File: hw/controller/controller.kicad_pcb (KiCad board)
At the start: 2 copper layers, 67.3 x 76.2 mm, 61 parts, among them J1 ARM-SWD, P1 USB_OTG, P10 GPIO, P11 VDD_SEL, P12 UART0, P13 SPI, P14 I2C0, P15 I2C1, P16 I2C2, P17 I2C3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

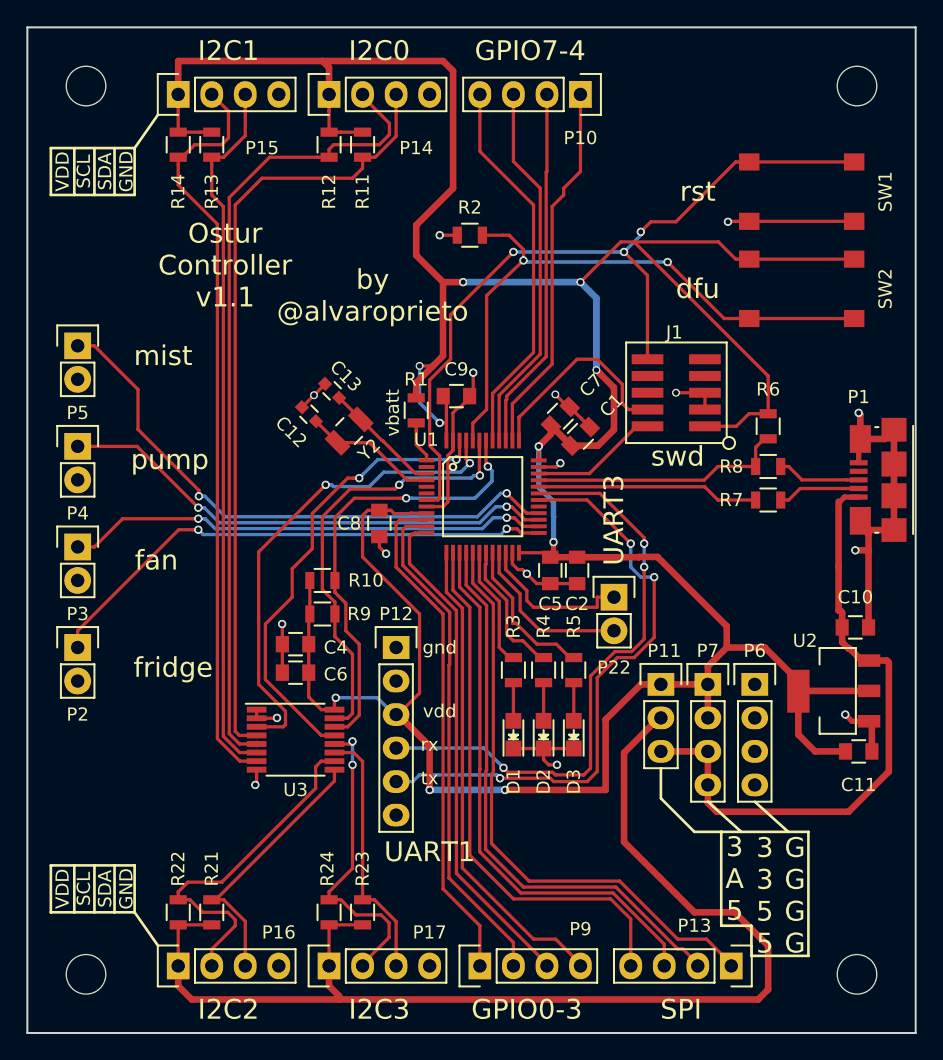
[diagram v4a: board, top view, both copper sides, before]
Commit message: Updating ostur controller!
Removed unused headers
Added extra shielding for 32768Hz crystal
Made board smaller
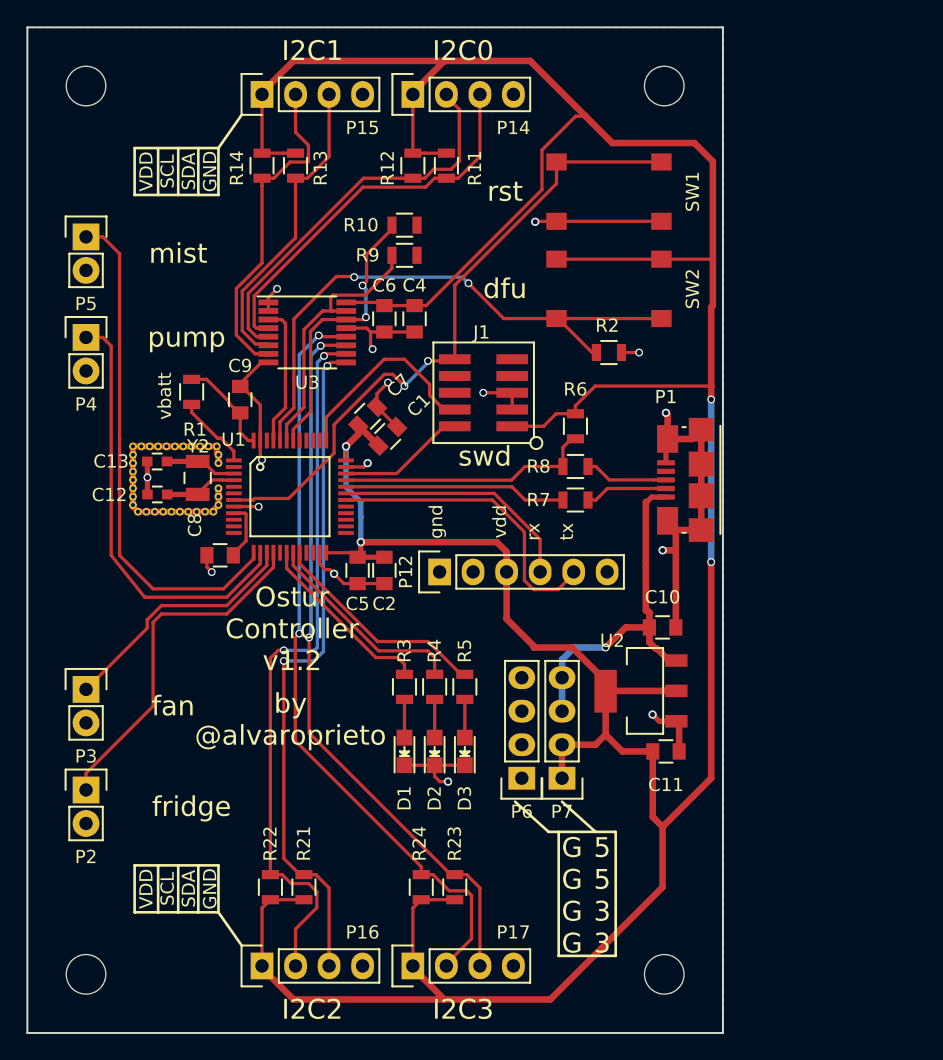
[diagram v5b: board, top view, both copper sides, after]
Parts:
- removed P10, P9: GPIO, Pin_Headers:Pin_Header_Straight_1x04
- removed P11: VDD_SEL, Pin_Headers:Pin_Header_Straight_1x03
- removed P13: SPI, Pin_Headers:Pin_Header_Straight_1x04
- removed P22: UART3, Pin_Headers:Pin_Header_Straight_1x02
- added REF**: via-0.6mm, footprints:via-0.6mm, F.Cu at (122.4, 109.2)
- added REF**: via-0.6mm, footprints:via-0.6mm, F.Cu at (117.9, 108.0)
- added REF**: via-0.6mm, footprints:via-0.6mm, F.Cu at (117.2, 108.0)
- added REF**: via-0.6mm, footprints:via-0.6mm, F.Cu at (116.6, 108.0)
- added REF**: via-0.6mm, footprints:via-0.6mm, F.Cu at (116.0, 108.0)
- added REF**: via-0.6mm, footprints:via-0.6mm, F.Cu at (116.0, 108.6)
- added REF**: via-0.6mm, footprints:via-0.6mm, F.Cu at (116.0, 109.2)
- added REF**: via-0.6mm, footprints:via-0.6mm, F.Cu at (116.0, 109.9)
- added REF**: via-0.6mm, footprints:via-0.6mm, F.Cu at (116.0, 110.5)
- added REF**: via-0.6mm, footprints:via-0.6mm, F.Cu at (116.0, 111.1)
- added REF**: via-0.6mm, footprints:via-0.6mm, F.Cu at (116.0, 111.8)
- added REF**: via-0.6mm, footprints:via-0.6mm, F.Cu at (122.4, 108.6)
- added REF**: via-0.6mm, footprints:via-0.6mm, F.Cu at (116.0, 112.4)
- added REF**: via-0.6mm, footprints:via-0.6mm, F.Cu at (116.3, 112.9)
- added REF**: via-0.6mm, footprints:via-0.6mm, F.Cu at (117.0, 112.9)
- added REF**: via-0.6mm, footprints:via-0.6mm, F.Cu at (117.6, 112.9)
- added REF**: via-0.6mm, footprints:via-0.6mm, F.Cu at (118.2, 112.9)
- added REF**: via-0.6mm, footprints:via-0.6mm, F.Cu at (118.9, 112.9)
- added REF**: via-0.6mm, footprints:via-0.6mm, F.Cu at (119.5, 112.9)
- added REF**: via-0.6mm, footprints:via-0.6mm, F.Cu at (120.1, 112.9)
- added REF**: via-0.6mm, footprints:via-0.6mm, F.Cu at (120.8, 112.9)
- added REF**: via-0.6mm, footprints:via-0.6mm, F.Cu at (122.0, 112.9)
- added REF**: via-0.6mm, footprints:via-0.6mm, F.Cu at (122.3, 108.0)
- added REF**: via-0.6mm, footprints:via-0.6mm, F.Cu at (122.4, 112.4)
- added REF**: via-0.6mm, footprints:via-0.6mm, F.Cu at (122.4, 111.8)
- added REF**: via-0.6mm, footprints:via-0.6mm, F.Cu at (122.4, 111.1)
- added REF**: via-0.6mm, footprints:via-0.6mm, F.Cu at (121.4, 112.9)
- added REF**: via-0.6mm, footprints:via-0.6mm, F.Cu at (121.7, 108.0)
- added REF**: via-0.6mm, footprints:via-0.6mm, F.Cu at (121.0, 108.0)
- added REF**: via-0.6mm, footprints:via-0.6mm, F.Cu at (120.4, 108.0)
- added REF**: via-0.6mm, footprints:via-0.6mm, F.Cu at (119.8, 108.0)
- added REF**: via-0.6mm, footprints:via-0.6mm, F.Cu at (119.1, 108.0)
- added REF**: via-0.6mm, footprints:via-0.6mm, F.Cu at (118.5, 108.0)
- C12, C13: value 12pF -> 6pF
- moved U3 30.9 mm to (129.2, 99.3)
- moved R9 27.9 mm to (136.5, 93.5), turned to 180 degrees
- moved C6 27.6 mm to (135.0, 98.3), turned to 270 degrees
- moved R10 27.6 mm to (136.5, 91.2), turned to 180 degrees
- moved C4 26.3 mm to (137.3, 98.3), turned to 270 degrees
- moved P6 19.0 mm to (145.4, 133.1), turned to 180 degrees
- moved R1 17.1 mm to (120.4, 103.8)
- moved C9 16.4 mm to (124.1, 104.4), turned to 90 degrees
- moved C1 14.6 mm to (135.3, 107.2)
- moved C11 14.6 mm to (156.3, 131.1)
- moved C5 14.6 mm to (133.0, 117.3)
- moved C7 14.6 mm to (133.7, 105.7)
- moved P1 14.6 mm to (156.3, 110.5)
- moved C10 14.6 mm to (156.1, 121.7)
- moved C2 14.6 mm to (135.0, 117.3)
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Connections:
- P16 pad 1: /VDD_ALT -> VDD
- P17 pad 1: /VDD_ALT -> VDD
- R21 pad 1: /VDD_ALT -> VDD
- R22 pad 1: /VDD_ALT -> VDD
- R23 pad 1: /VDD_ALT -> VDD
- R24 pad 1: /VDD_ALT -> VDD
- U1 pad 10: /GPIO0 -> Net-(U1-Pad10)
- U1 pad 11: /GPIO1 -> Net-(U1-Pad11)
- U1 pad 12: /GPIO2 -> Net-(U1-Pad12)
- U1 pad 13: /GPIO3 -> /MIST
- U1 pad 14: /CS -> /PUMP
- U1 pad 15: /SCK -> /FAN
- U1 pad 16: /MISO -> /FRIDGE
- U1 pad 17: /MOSI -> Net-(U1-Pad17)
- U1 pad 21: /UART3_TX -> Net-(U1-Pad21)
- U1 pad 22: /UART3_RX -> Net-(U1-Pad22)
- U1 pad 25: /FRIDGE -> Net-(U1-Pad25)
- U1 pad 26: /FAN -> Net-(U1-Pad26)
- U1 pad 27: /PUMP -> Net-(U1-Pad27)
- U1 pad 28: /MIST -> Net-(U1-Pad28)
- U1 pad 38: /GPIO4 -> Net-(U1-Pad38)
- U1 pad 39: /GPIO5 -> Net-(U1-Pad39)
- U1 pad 40: /GPIO6 -> Net-(U1-Pad40)
- U1 pad 41: /GPIO7 -> Net-(U1-Pad41)
- U1 pad 46: /TCA_A2 -> Net-(U1-Pad46)
- U3 pad 13: /TCA_A2 -> GND
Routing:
- net /VDD_ALT: track 89.3 -> 0.00 mm
- net /MOSI: track 44.8 -> 0.00 mm
- net /MISO: track 43.0 -> 0.00 mm
- net /SCK: track 41.8 -> 0.00 mm
- net /CS: track 41.2 -> 0.00 mm
- net /GPIO0: track 38.6 -> 0.00 mm
- net /GPIO1: track 38.5 -> 0.00 mm
- net /GPIO2: track 38.2 -> 0.00 mm
- net /GPIO3: track 36.5 -> 0.00 mm
- net /SDA3: track 19.5 -> 55.4 mm, vias 0 -> 2
- net /TCA_A2: track 35.2 -> 0.00 mm, vias 2 -> 0
- net /SCL3: track 23.6 -> 58.3 mm
- net /SCL1: track 57.5 -> 25.2 mm
- net /SDA2: track 20.5 -> 51.8 mm, vias 0 -> 2
- net /SCL0: track 61.4 -> 30.0 mm
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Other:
- board size 67.3 x 76.2 mm -> 52.7 x 76.2 mm
- board text added: "5 5 3 3"
- board text added: "Ostur Controller v1.2"
- board text removed: "3 3 5 5"
- board text removed: "3 A 5"
- board text removed: "GPIO0-3"
- board text removed: "GPIO7-4"
- board text removed: "Ostur Controller v1.1"
- board text removed: "SPI"
- board text removed: "UART1"
- board text removed: "UART3"

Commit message: Fixed controller PCB...
Somehow I forgot to connect some VDD lines on the micocontroller.....
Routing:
- net VDD: track 303.8 -> 325.5 mm, vias 4 -> 6
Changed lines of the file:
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@@
-(kicad_pcb (version 4) (host pcbnew 4.0.2+dfsg1-stable)
+(kicad_pcb (version 4) (host pcbnew 4.0.6-e0-6349~53~ubuntu16.04.1)
   (general
     (links 173)
-    (no_connects 4)
-    (area 107.874999 76.124999 160.730001 152.475001)
+    (no_connects 0)
+    (area 105.981474 75.6695 164.625046 154.03126)
     (thickness 1.6)
     (drawings 49)
-    (tracks 548)
+    (tracks 563)
     (zones 0)
     (modules 89)
@@
   (gr_line (start 160.655 152.4) (end 107.95 152.4) (layer Edge.Cuts) (width 0.15))
   (gr_line (start 160.655 76.2) (end 160.655 152.4) (layer Edge.Cuts) (width 0.15))
+  (segment (start 137.475 93.472) (end 137.475 91.186) (width 0.25) (layer F.Cu) (net 1))
+  (segment (start 137.287 97.282) (end 137.287 93.66) (width 0.25) (layer F.Cu) (net 1))
+  (segment (start 137.287 93.66) (end 137.475 93.472) (width 0.25) (layer F.Cu) (net 1))
+  (segment (start 124.719 113.284) (end 127 113.284) (width 0.25) (layer F.Cu) (net 1))
+  (segment (start 127 113.284) (end 129.54 113.284) (width 0.25) (layer F.Cu) (net 1))
+  (segment (start 127 112.776) (end 127 113.284) (width 0.25) (layer F.Cu) (net 1))
+  (segment (start 127 110.998) (end 127 112.776) (width 0.25) (layer B.Cu) (net 1))
+  (via (at 127 112.776) (size 0.6) (drill 0.4) (layers F.Cu B.Cu) (net 1))
+  (segment (start 125.095 110.109) (end 125.984 110.998) (width 0.25) (layer F.Cu) (net 1))
+  (segment (start 125.984 110.998) (end 127 110.998) (width 0.25) (layer F.Cu) (net 1))
+  (via (at 127 110.998) (size 0.6) (drill 0.4) (layers F.Cu B.Cu) (net 1))
+  (segment (start 125.095 107.51) (end 125.095 110.109) (width 0.25) (layer F.Cu) (net 1))
+  (segment (start 129.54 113.284) (end 130.595 114.339) (width 0.25) (layer F.Cu) (net 1))
+  (segment (start 130.595 114.339) (end 130.595 116.01) (width 0.25) (layer F.Cu) (net 1))
+  (segment (start 124.445 113.01) (end 124.719 113.284) (width 0.25) (layer F.Cu) (net 1))
   (segment (start 120.396 102.87) (end 121.539 102.87) (width 0.25) (layer F.Cu) (net 1))
   (segment (start 121.539 102.87) (end 123.204 104.535) (width 0.25) (layer F.Cu) (net 1))

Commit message: Fix merge screwup
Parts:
- removed P1: USB_OTG, footprints:USB_MICRO_B
- added J2: USB_OTG, footprints:USB_MICRO_B, F.Cu at (156.5, 110.5)

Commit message: Adding cheese wedges!
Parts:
- removed P12: UART0, Pin_Headers:Pin_Header_Straight_1x06
- added C14: 100nF, Capacitors_SMD:C_0603, F.Cu at (128.6, 86.6)
- added C15: 100nF, Capacitors_SMD:C_0603, F.Cu at (135.1, 118.3)
- added C16: 100nF, Capacitors_SMD:C_0603, F.Cu at (121.5, 97.6)
- added C17: 100nF, Capacitors_SMD:C_0603, F.Cu at (238.8, 72.4)
- added C3: 100nF, Capacitors_SMD:C_0603, F.Cu at (124.6, 111.0)
- added J3: UART, Pin_Headers:Pin_Header_Straight_1x03_Pitch1.27mm, F.Cu at (170.2, 90.2)
- added P1: TH0, Pin_Headers:Pin_Header_Straight_1x04_Pitch2.54mm, F.Cu at (105.7, 112.0)
- added P8: TH3, Pin_Headers:Pin_Header_Straight_1x04_Pitch2.54mm, F.Cu at (108.8, 83.4)
- added R15: 10k, Resistors_SMD:R_0603, F.Cu at (121.1, 109.6)
- added R16: DNP, Resistors_SMD:R_0603, F.Cu at (131.6, 82.5)
- added R17: 10k, Resistors_SMD:R_0603, F.Cu at (129.9, 83.3)
- added R18: DNP, Resistors_SMD:R_0603, F.Cu at (129.8, 118.6)
- added R19: 10k, Resistors_SMD:R_0603, F.Cu at (131.5, 119.4)
- added R20: DNP, Resistors_SMD:R_0603, F.Cu at (121.2, 92.3)
- added R25: 10k, Resistors_SMD:R_0603, F.Cu at (120.4, 94.0)
- added R26: DNP, Resistors_SMD:R_0603, F.Cu at (240.8, 83.8)
- added R27: DNP, Resistors_SMD:R_0603, F.Cu at (240.8, 80.0)
- added U4: SHT3x-DIS, footprints:SHT3x, F.Cu at (124.9, 107.1)
- added U5: SHT3x-DIS, footprints:SHT3x, F.Cu at (132.5, 87.0)
- added U6: SHT3x-DIS, footprints:SHT3x, F.Cu at (132.8, 115.1)
- added U7: SHT3x-DIS, footprints:SHT3x, F.Cu at (124.7, 95.4)
- added U8: SHT3x-DIS, footprints:SHT3x, F.Cu at (233.7, 72.4)
- C1, C2, C4, C5, C6, C7, C8, C9: footprint Capacitors_SMD:C_0805 -> Capacitors_SMD:C_0603
- C10: value 100nF -> 1uF; footprint Capacitors_SMD:C_0805 -> Capacitors_SMD:C_0603
- C11: value 10uF -> 1uF; footprint Capacitors_SMD:C_0805 -> Capacitors_SMD:C_0603
- D1, D2, D3: footprint LEDs:LED_0805 -> LEDs:LED_0603
- J1, SW1, SW2: moved to B.Cu
- P6: value GND -> TH1; footprint Pin_Headers:Pin_Header_Straight_1x04 -> Pin_Headers:Pin_Header_Straight_1x04_Pitch2.54mm
- P7: value VDD -> TH2; footprint Pin_Headers:Pin_Header_Straight_1x04 -> Pin_Headers:Pin_Header_Straight_1x04_Pitch2.54mm
- R1, R10, R11, R12, R13, R14, R2, R21, R22, R23, R24, R3, R4, R5, R7, R8, R9: footprint Resistors_SMD:R_0805 -> Resistors_SMD:R_0603
- R6: value 1.5k -> DNP; footprint Resistors_SMD:R_0805 -> Resistors_SMD:R_0603
- U2: value LDO -> MIC550X; footprint footprints:SOT-223 -> footprints:SOT-23(M5)
- moved R9 143.7 mm to (261.3, 164.8), turned to 0 degrees
- moved R10 140.6 mm to (248.3, 176.5), turned to 0 degrees
- moved R1 138.7 mm to (238.4, 176.6), turned to 0 degrees
- moved C9 135.5 mm to (244.5, 166.5), turned to 0 degrees
- moved C7 133.9 mm to (260.1, 149.8), turned to 0 degrees
- moved D3 133.9 mm to (272.9, 154.5), turned to 0 degrees
- moved D2 133.2 mm to (269.5, 157.2), turned to 0 degrees
- moved R8 129.3 mm to (272.3, 149.7), turned to 0 degrees
- moved C6 129.2 mm to (247.7, 161.5), turned to 0 degrees
- moved C8 128.7 mm to (243.6, 160.0), turned to 0 degrees
- moved C5 126.6 mm to (255.3, 149.8), turned to 0 degrees
- moved R4 126.1 mm to (261.6, 154.9), turned to 0 degrees
- moved D1 125.2 mm to (255.1, 171.3), turned to 0 degrees
- moved C1 122.7 mm to (247.7, 156.4), turned to 0 degrees
- moved R3 121.7 mm to (251.3, 166.5), turned to 0 degrees
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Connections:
- P6 pad 1: GND -> /VDD_TH1
- P6 pad 2: GND -> /SCL_TH1
- P6 pad 3: GND -> /SDA_TH1
- P6 pad 4: GND -> /GND_TH1
- P7 pad 1: VDD -> /VDD_TH2
- P7 pad 2: VDD -> /SCL_TH2
- P7 pad 3: +5V -> /SDA_TH2
- P7 pad 4: +5V -> /GND_TH2
- R6 pad 1: VDD -> /ADDR_TH0
- R6 pad 2: /USB_DP -> /VDD_TH0
- U2 pad 1: GND -> +5V
- U2 pad 2: VDD -> GND
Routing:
- net VDD: track 325.5 -> 0.00 mm, vias 6 -> 0
- net GND: track 109.7 -> 22.9 mm, vias 16 -> 1
- net /SCL3: track 58.3 -> 0.00 mm, vias 2 -> 0
- net /SDA3: track 55.4 -> 0.00 mm, vias 2 -> 0
- net /SCL2: track 54.7 -> 0.00 mm, vias 2 -> 0
- net /SDA2: track 51.8 -> 0.00 mm, vias 2 -> 0
- net /nRST: track 49.3 -> 0.00 mm, vias 2 -> 0
- net /boot0: track 44.2 -> 0.00 mm, vias 2 -> 0
- net /MIST: track 38.7 -> 0.00 mm
- net /PUMP: track 32.7 -> 0.00 mm
- net /VDD_TH0: track 0.00 -> 31.7 mm
- net /VDD_TH3: track 0.00 -> 31.6 mm
- net /VDD_TH2: track 0.00 -> 31.2 mm
- net /VDD_TH1: track 0.00 -> 30.4 mm
- net /SCL0: track 30.0 -> 0.00 mm
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- removed copper zone on B.Cu, net GND
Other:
- board size 52.7 x 76.2 mm -> 77.5 x 76.2 mm
- net class Default: clearance 0.2 -> 0.1524; trace_width 0.25 -> 0.1524; via_dia 0.6 -> 0.6858; via_drill 0.4 -> 0.3302
- rule trace_clearance: 0.2 -> 0.1524
- rule via_min_drill: 0 -> 0.3302
- rule via_min_size: 0.4 -> 0.6858
- board text removed: "5 5 3 3"
- board text removed: "G G G G"
- board text removed: "fan"
- board text removed: "fridge"
- board text removed: "gnd"
- board text removed: "mist"
- board text removed: "pump"
- board text removed: "rx"
- board text removed: "tx"
- board text removed: "vbatt"
- board text removed: "vdd"
